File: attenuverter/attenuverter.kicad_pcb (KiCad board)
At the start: 2 copper layers, 71.9 x 168.7 mm, 89 parts, among them J1 Power, J10 Conn_01x03_Socket, J11 Output 1, J12 Input 1, J13 Conn_01x03_Socket, J14 Conn_01x03_Socket, J15 Output 1, J16 Input 1, J17 Conn_01x03_Socket, J18 Conn_01x03_Socket, J19 Output 1, J2 Power, J3 Power, J4 Input 1, J5 Conn_01x03_Socket, J6 Conn_01x03_Socket, J7 Output 1, J8 Input 1, J9 Conn_01x03_Socket, U1 TL074, U2 TL074, U3 TL074

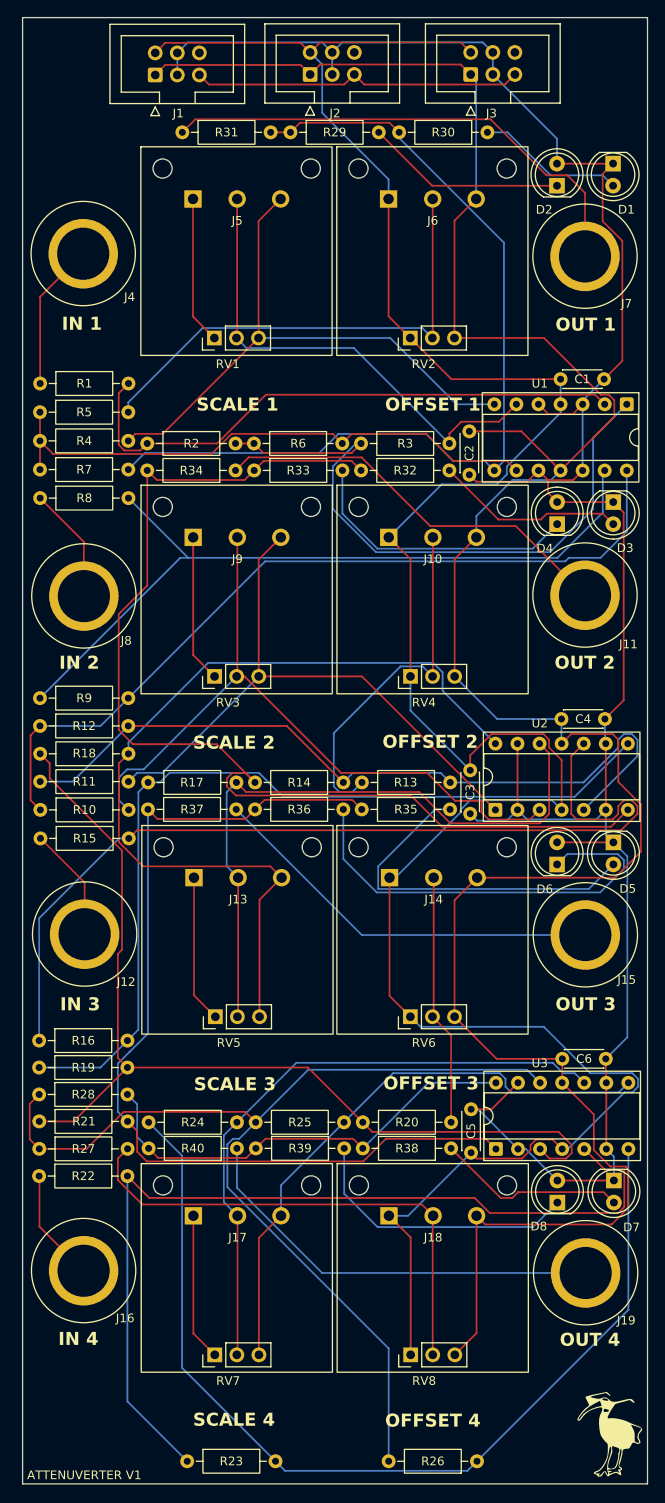
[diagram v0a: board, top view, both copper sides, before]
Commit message: Fix attenuverter
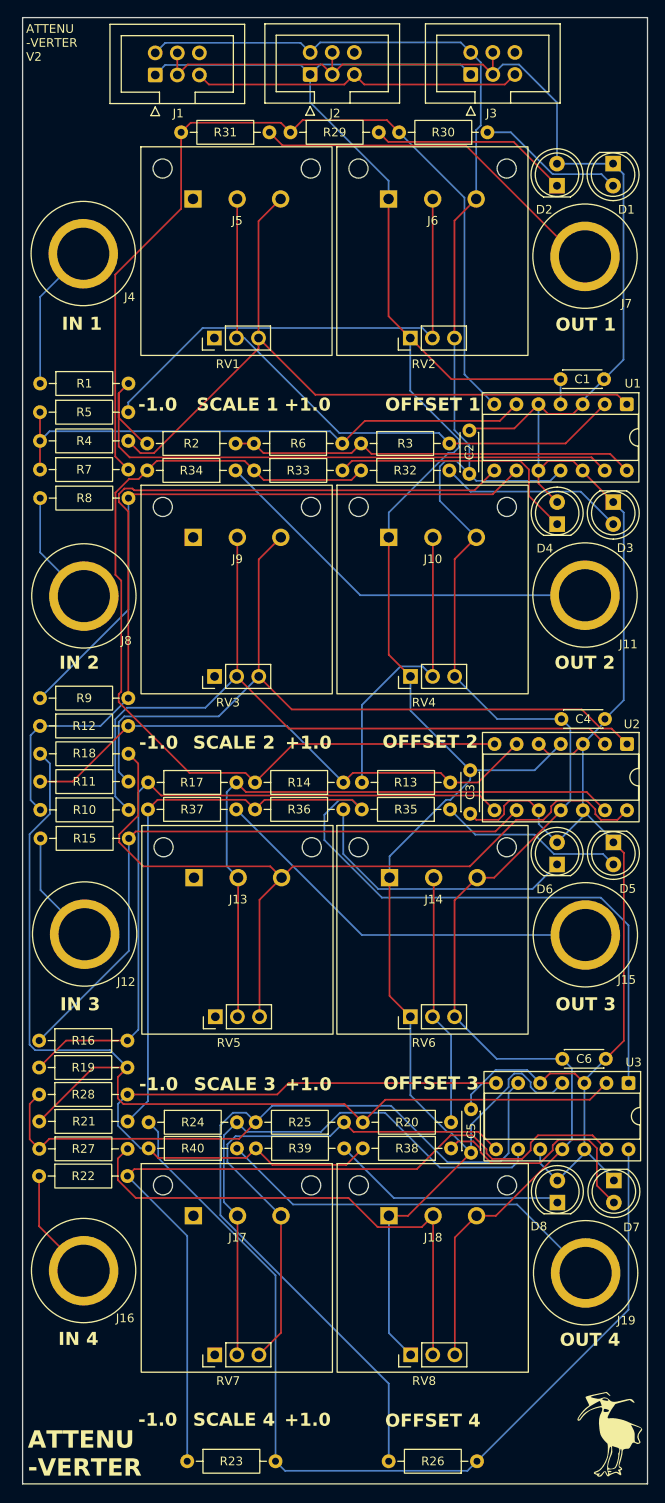
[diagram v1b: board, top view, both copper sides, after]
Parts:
- moved U3 17.0 mm to (90.0, 140.7), turned to -90 degrees
- moved U2 16.9 mm to (89.8, 101.7), turned to -90 degrees
- moved R31 10.0 mm to (48.7, 31.3), turned to 180 degrees
- moved C2 4.90 mm to (71.7, 70.6), turned to 90 degrees
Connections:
- C1 pad 2: -12V -> 12V
- C2 pad 1: 12V -> -12V
- C3 pad 2: -12V -> 12V
- C4 pad 1: 12V -> -12V
- C5 pad 2: -12V -> 12V
- C6 pad 1: 12V -> -12V
- J10 pad 1: -12V -> 12V
- J10 pad 3: 12V -> -12V
- J14 pad 1: -12V -> 12V
- J14 pad 3: 12V -> -12V
- J18 pad 1: -12V -> 12V
- J18 pad 3: 12V -> -12V
- J6 pad 1: -12V -> 12V
- J6 pad 3: 12V -> -12V
- R1 pad 2: Net-(U1A--) -> Net-(U1D--)
- R11 pad 2: Net-(U2B-+) -> Net-(U2B--)
- R12 pad 2: Net-(U2B-+) -> Net-(U2B--)
- R13 pad 1: Net-(U2B-+) -> Net-(U2B--)
- R14 pad 1: Net-(U2B-+) -> Net-(U2B--)
- R15 pad 2: Net-(U2C-+) -> Net-(U2C--)
- R16 pad 1: Net-(U2C-+) -> Net-(U2C--)
- R18 pad 2: Net-(U3A-+) -> Net-(U3A--)
- R19 pad 2: Net-(U3A-+) -> Net-(U3A--)
- R2 pad 1: Net-(U1A--) -> Net-(U1D--)
- R20 pad 1: Net-(U3A-+) -> Net-(U3A--)
- R21 pad 1: Net-(U3A-+) -> Net-(U3A--)
- R22 pad 2: Net-(U3B-+) -> Net-(U3D--)
- R23 pad 1: Net-(U3B-+) -> Net-(U3D--)
- R25 pad 2: Net-(U3D-+) -> Net-(U3B--)
- R26 pad 2: Net-(U3D-+) -> Net-(U3B--)
- R27 pad 1: Net-(U3D-+) -> Net-(U3B--)
- R28 pad 1: Net-(U3D-+) -> Net-(U3B--)
- R4 pad 2: Net-(U1C--) -> Net-(U1B--)
- R5 pad 1: Net-(U1C--) -> Net-(U1B--)
- R6 pad 2: Net-(U1C--) -> Net-(U1B--)
- R7 pad 1: Net-(U1C--) -> Net-(U1B--)
- R8 pad 2: Net-(U1D--) -> Net-(U1C--)
- R9 pad 1: Net-(U1D--) -> Net-(U1C--)
- RV1 pad 1: unconnected-(J5-Pin_1-Pad1) -> unconnected-(RV1-Pad1)
- RV2 pad 1: -12V -> 12V
- RV2 pad 3: 12V -> -12V
- RV3 pad 1: unconnected-(J9-Pin_1-Pad1) -> unconnected-(RV3-Pad1)
- RV4 pad 1: -12V -> 12V
- RV4 pad 3: 12V -> -12V
- RV5 pad 1: unconnected-(J13-Pin_1-Pad1) -> unconnected-(RV5-Pad1)
- RV6 pad 1: -12V -> 12V
- RV6 pad 3: 12V -> -12V
- RV7 pad 1: unconnected-(J17-Pin_1-Pad1) -> unconnected-(RV7-Pad1)
- RV8 pad 1: -12V -> 12V
- RV8 pad 3: 12V -> -12V
- U1 pad 1: Net-(R2-Pad2) -> Net-(J5-Pin_3)
- U1 pad 11: 12V -> -12V
- U1 pad 14: Net-(R10-Pad1) -> Net-(R2-Pad2)
- U1 pad 2: Net-(U1A--) -> Net-(J5-Pin_2)
- U1 pad 4: -12V -> 12V
- U1 pad 6: Net-(J5-Pin_2) -> Net-(U1B--)
- U1 pad 7: Net-(J5-Pin_3) -> Net-(R29-Pad1)
- U1 pad 8: Net-(R29-Pad1) -> Net-(R10-Pad1)
- U2 pad 10: Net-(U2C-+) -> GND
- U2 pad 11: 12V -> -12V
- U2 pad 12: Net-(J13-Pin_2) -> GND
- U2 pad 13: GND -> Net-(J13-Pin_2)
- U2 pad 2: GND -> Net-(J9-Pin_2)
- U2 pad 3: Net-(J9-Pin_2) -> GND
- U2 pad 4: -12V -> 12V
- U2 pad 5: Net-(U2B-+) -> GND
- U2 pad 6: GND -> Net-(U2B--)
- U2 pad 9: GND -> Net-(U2C--)
- U3 pad 10: Net-(J17-Pin_2) -> GND
- U3 pad 11: 12V -> -12V
- U3 pad 12: Net-(U3D-+) -> GND
- U3 pad 13: GND -> Net-(U3D--)
- U3 pad 14: Net-(R28-Pad2) -> Net-(R23-Pad2)
- U3 pad 2: GND -> Net-(U3A--)
- U3 pad 3: Net-(U3A-+) -> GND
- U3 pad 4: -12V -> 12V
- U3 pad 5: Net-(U3B-+) -> GND
- U3 pad 6: GND -> Net-(U3B--)
- U3 pad 7: Net-(R23-Pad2) -> Net-(R28-Pad2)
- U3 pad 9: GND -> Net-(J17-Pin_2)
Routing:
- net Net-(U3B--): track 0.00 -> 126.7 mm
- net Net-(U3A--): track 0.00 -> 123.2 mm
- net Net-(U3D-+): track 118.6 -> 0.00 mm
- net Net-(U3A-+): track 113.5 -> 0.00 mm
- net Net-(U2C-+): track 107.1 -> 0.00 mm
- net Net-(U3B-+): track 104.7 -> 0.00 mm
- net Net-(U3D--): track 0.00 -> 96.4 mm
- net Net-(U2B-+): track 88.7 -> 0.00 mm
- net Net-(U2C--): track 0.00 -> 73.5 mm
- net Net-(U1A--): track 66.8 -> 0.00 mm
- net Net-(U1B--): track 0.00 -> 64.3 mm
- net Net-(U2B--): track 0.00 -> 62.9 mm
- net -12V: track 301.4 -> 243.1 mm
- net Net-(R28-Pad2): track 52.1 -> 78.7 mm
- net 12V: track 292.4 -> 266.8 mm
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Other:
- board text added: "+1.0"
- board text added: "-1.0"
- board text added: "ATTENU -VERTER"
- board text added: "ATTENU -VERTER V2"
- board text removed: "ATTENUVERTER V1"

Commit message: Vca fixes
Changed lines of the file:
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@@
 	)
 	(gr_text "ATTENU\n-VERTER\nV2"
-		(at 20.7 21 0)
+		(at 24 21 0)
 		(layer "F.SilkS")
 		(effects
@@
 				(thickness 0.15)
 			)
-			(justify left)
 		)
 	)
